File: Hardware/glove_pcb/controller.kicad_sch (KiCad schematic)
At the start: 30 parts, among them J11 61300611121, J12 67997-206HLF, J13 22053061, U12 MCP3008, U13 ATmega328PB-A, U14 MCP3008, U15 MCP3008

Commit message: Reworking placing
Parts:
- renumbered J11 to J7, J12 to J8, J13 to J9

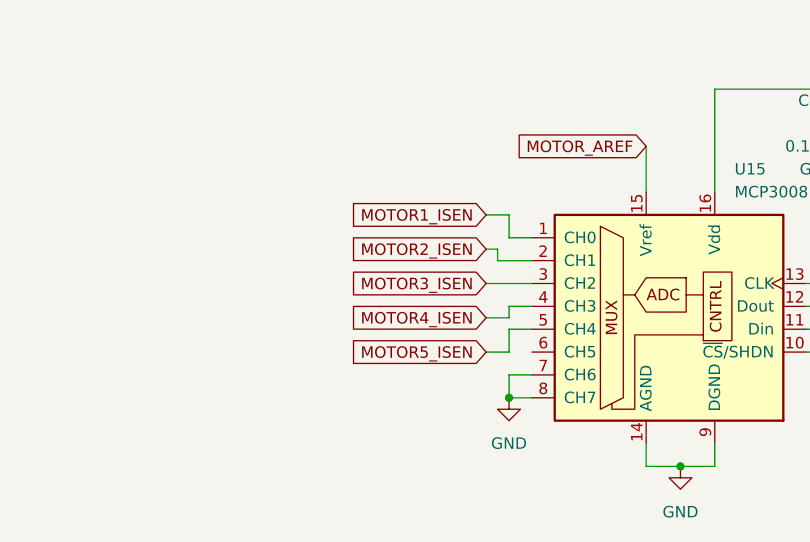
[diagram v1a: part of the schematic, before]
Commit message: Did the Routing for PCB
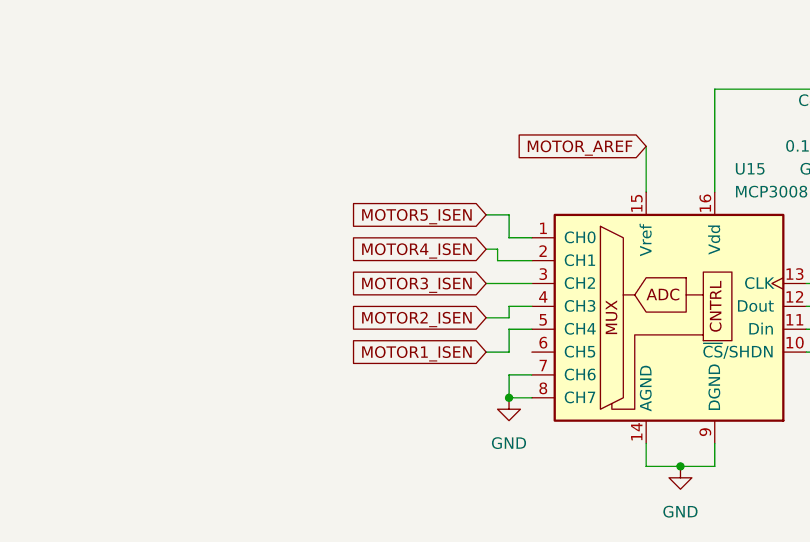
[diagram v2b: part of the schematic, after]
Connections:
- net MOTOR1_ISEN: now also U15.5 (CH4); no longer U15.1 (CH0)
- net MOTOR2_ISEN: now also U15.4 (CH3); no longer U15.2 (CH1)
- net MOTOR4_ISEN: now also U15.2 (CH1); no longer U15.4 (CH3)
- net MOTOR5_ISEN: now also U15.1 (CH0); no longer U15.5 (CH4)

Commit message: Changes before/after meeting w Dimitry
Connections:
- net GND: now also U15.6 (CH5)
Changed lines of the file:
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@@
   (junction (at 190.5 161.29) (diameter 0) (color 0 0 0 0)
+  )
+  (junction (at 106.68 166.37) (diameter 0) (color 0 0 0 0)
   )
   (junction (at 190.5 130.81) (diameter 0) (color 0 0 0 0)
@@
     (stroke (width 0) (type default))
   )
+  (wire (pts (xy 106.68 163.83) (xy 106.68 166.37))
+    (stroke (width 0) (type default))
+  )

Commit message: More intermediate changes
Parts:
- added C41: 10uF, Capacitor_SMD:C_1206_3216Metric_Pad1.33x1.80mm_HandSolder, symbol Device:C
- renumbered C41 to C42, C42 to C43, C43 to C44, C44 to C45, C45 to C46, C46 to C47, C47 to C48, C48 to C49, C49 to C50, C50 to C51, C51 to C52
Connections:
- net +5V: now also C41.2
- net GND: now also C41.1

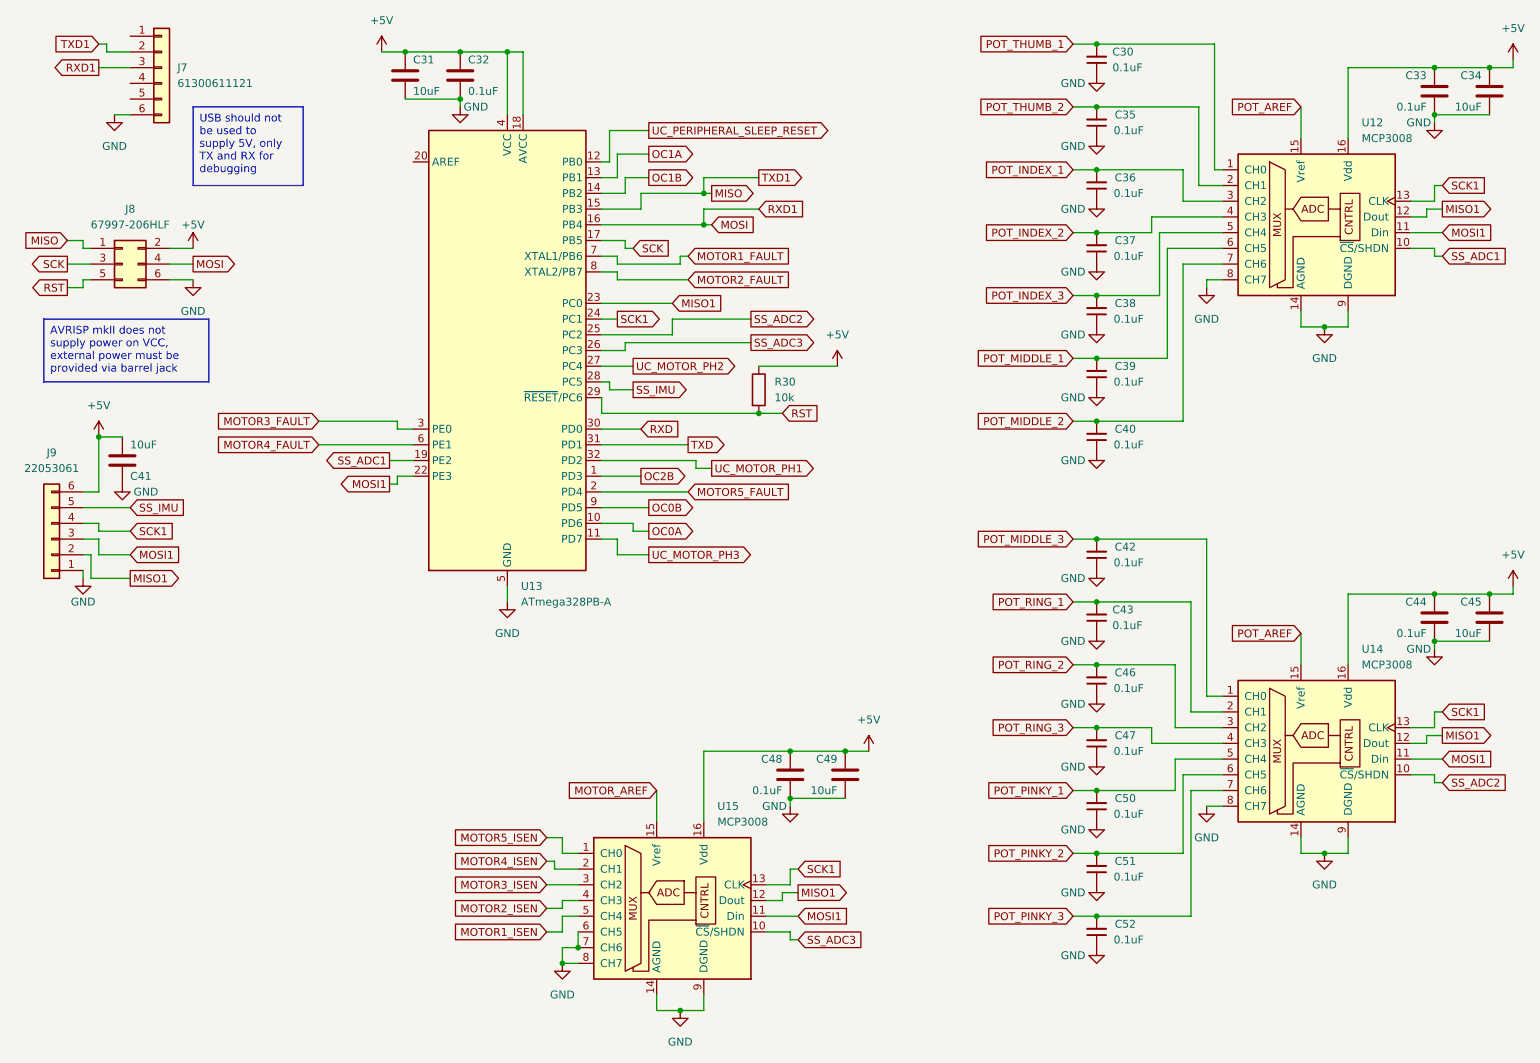
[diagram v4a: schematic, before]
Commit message: More improvements and routing fixes
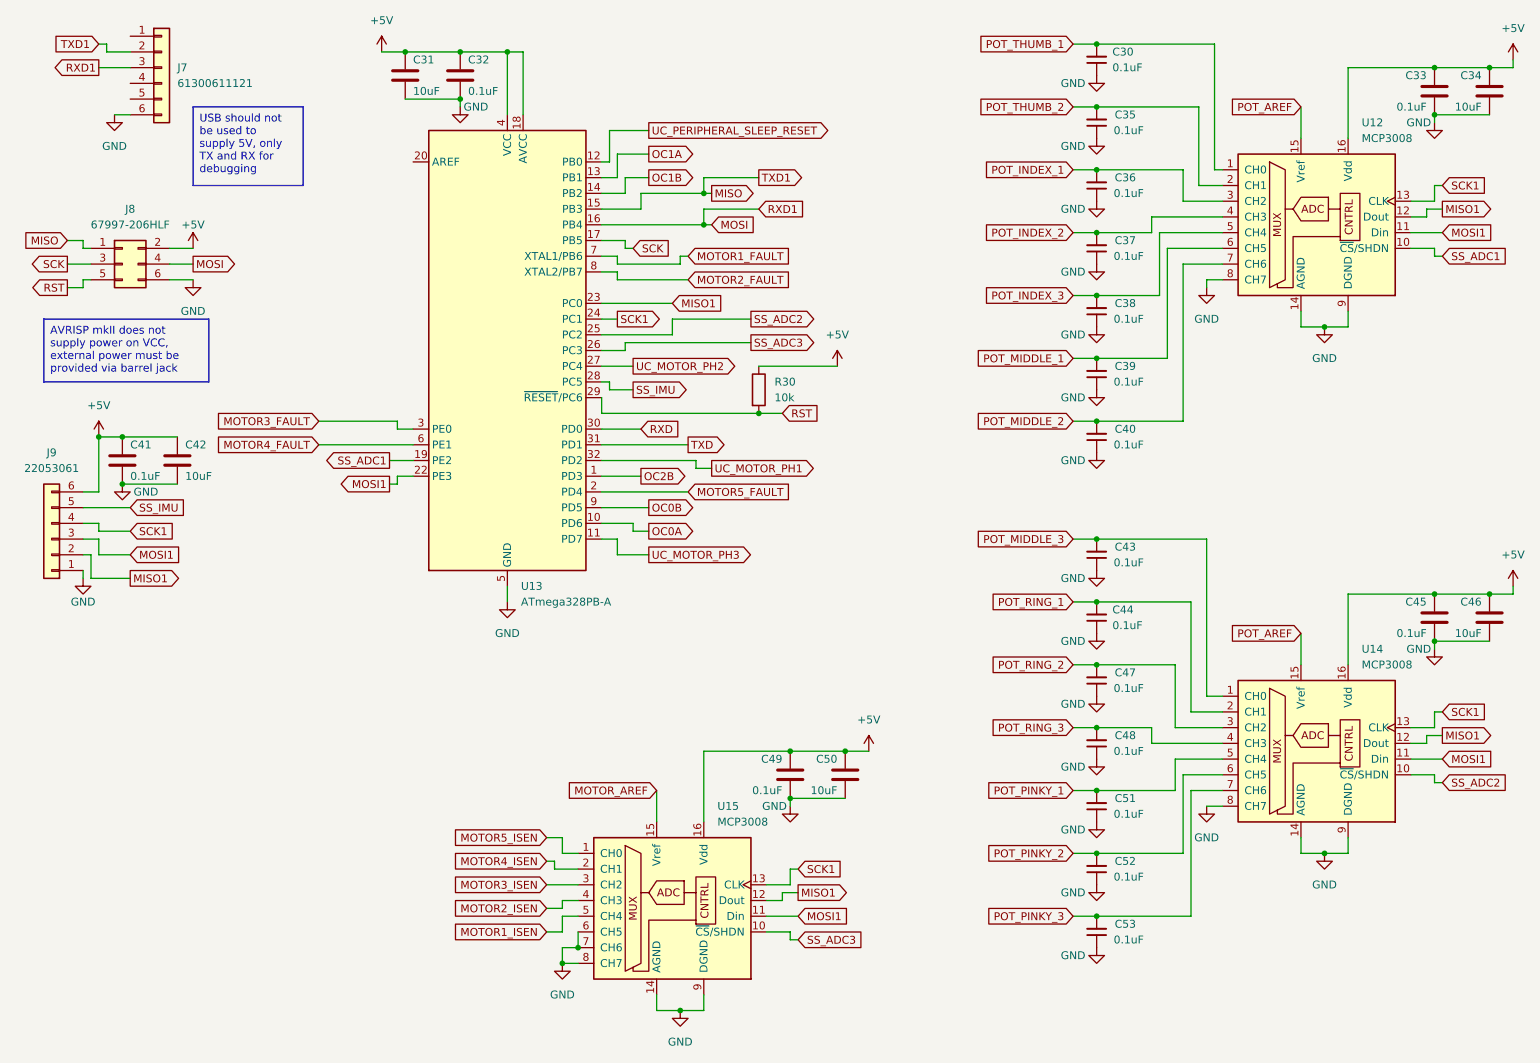
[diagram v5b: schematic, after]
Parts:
- added C42: 10uF, Capacitor_SMD:C_1206_3216Metric_Pad1.33x1.80mm_HandSolder, symbol Device:C
- C41: value 10uF -> 0.1uF; footprint Capacitor_SMD:C_1206_3216Metric_Pad1.33x1.80mm_HandSolder -> Capacitor_SMD:C_0603_1608Metric_Pad1.08x0.95mm_HandSolder
- renumbered C42 to C43, C43 to C44, C44 to C45, C45 to C46, C46 to C47, C47 to C48, C48 to C49, C49 to C50, C50 to C51, C51 to C52, C52 to C53
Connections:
- net +5V: now also C41.1, C42.1; no longer C41.2
- net GND: now also C41.2, C42.2; no longer C41.1
